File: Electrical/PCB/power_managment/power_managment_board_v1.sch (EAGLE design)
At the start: 0 parts

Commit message: Started schematic for boost converter
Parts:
- added U$1: LMR64010SOT, RobotRacing2019_Master:LMR64010SOT

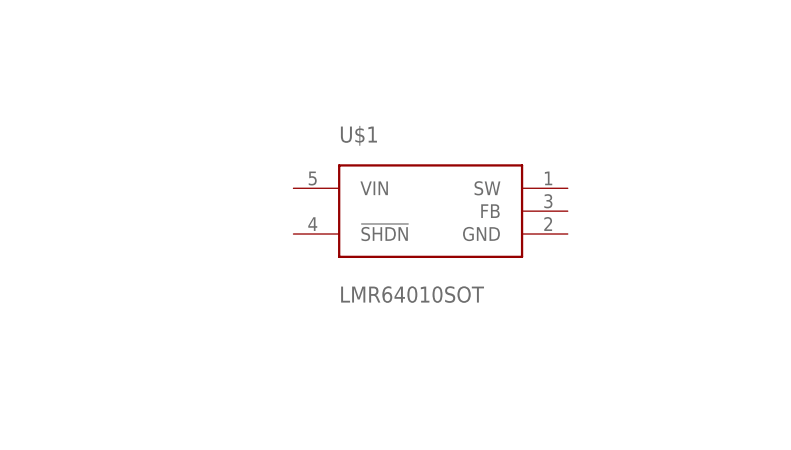
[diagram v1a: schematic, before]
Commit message: Imported a diode library
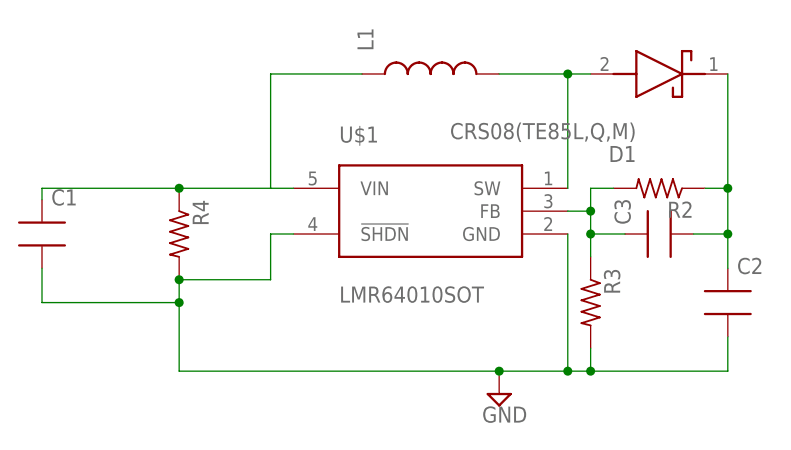
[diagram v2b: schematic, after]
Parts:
- added C1, C2, C3: (no value), RobotRacing2019_Master:CAP0603
- added D1: CRS08(TE85L,Q,M), SamacSys_Parts:CRS08(TE85L,Q,M)
- added L1: (no value), RobotRacing2019_Master:IND0603
- added R2, R3, R4: (no value), RobotRacing2019_Master:RES0603
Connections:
- new net GND: C1.2, C2.2, R3.2, R4.2, U$1.!SHDN, U$1.GND
- new net N$1: C1.1, L1.1, R4.1, U$1.VIN
- new net N$2: C2.1, C3.2, D1.K, R2.1
- new net N$3: C3.1, R2.2, R3.1, U$1.FB
- new net N$4: D1.A, L1.2, U$1.SW
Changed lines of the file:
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@@
 <parts>
 <part name="U$1" library="RobotRacing2019_Master" deviceset="LMR64010" device="SOT"/>
+<part name="C1" library="RobotRacing2019_Master" deviceset="CAP0603" device=""/>
+<part name="C2" library="RobotRacing2019_Master" deviceset="CAP0603" device=""/>
+<part name="C3" library="RobotRacing2019_Master" deviceset="CAP0603" device=""/>
+<part name="R2" library="RobotRacing2019_Master" deviceset="RES0603" device=""/>
+<part name="R3" library="RobotRacing2019_Master" deviceset="RES0603" device=""/>
+<part name="R4" library="RobotRacing2019_Master" deviceset="RES0603" device=""/>
+<part name="SUPPLY1" library="RobotRacing2019_Master" deviceset="GND" device=""/>
+<part name="L1" library="RobotRacing2019_Master" deviceset="IND0603" device=""/>
+<part name="D1" library="SamacSys_Parts" deviceset="CRS08(TE85L,Q,M)" device=""/>
 </parts>
 <sheets>
@@
 <attribute name="VALUE" x="-10.16" y="-10.16" size="1.778" layer="96"/>
 </instance>
+<instance part="C1" gate="G$1" x="-43.18" y="-2.54" smashed="yes">
+<attribute name="NAME" x="-42.164" y="0.635" size="1.778" layer="95"/>
+<attribute name="VALUE" x="-42.164" y="-6.731" size="1.778" layer="96"/>
+</instance>
+<instance part="C2" gate="G$1" x="33.02" y="-10.16" smashed="yes">
+<attribute name="NAME" x="34.036" y="-6.985" size="1.778" layer="95"/>
+<attribute name="VALUE" x="34.036" y="-14.351" size="1.778" layer="96"/>
+</instance>
+<instance part="C3" gate="G$1" x="25.4" y="-2.54" smashed="yes" rot="R90">
+<attribute name="NAME" x="22.225" y="-1.524" size="1.778" layer="95" rot="R90"/>
+<attribute name="VALUE" x="29.591" y="-1.524" size="1.778" layer="96" rot="R90"/>
+</instance>
+<instance part="R2" gate="G$1" x="25.4" y="2.54" smashed="yes" rot="R180">
+<attribute name="NAME" x="29.21" y="1.0414" size="1.778" layer="95" rot="R180"/>
+<attribute name="VALUE" x="29.21" y="5.842" size="1.778" layer="96" rot="R180"/>
+</instance>
+<instance part="R3" gate="G$1" x="17.78" y="-10.16" smashed="yes" rot="R270">
+<attribute name="NAME" x="19.2786" y="-6.35" size="1.778" layer="95" rot="R270"/>
+<attribute name="VALUE" x="14.478" y="-6.35" size="1.778" layer="96" rot="R270"/>
+</instance>
+<instance part="R4" gate="G$1" x="-27.94" y="-2.54" smashed="yes" rot="R270">
+<attribute name="NAME" x="-26.4414" y="1.27" size="1.778" layer="95" rot="R270"/>
+<attribute name="VALUE" x="-31.242" y="1.27" size="1.778" layer="96" rot="R270"/>
+</instance>
+<instance part="SUPPLY1" gate="GND" x="7.62" y="-20.32" smashed="yes">
+<attribute name="VALUE" x="5.715" y="-23.495" size="1.778" layer="96"/>
+</instance>
+<instance part="L1" gate="G$1" x="0" y="15.24" smashed="yes" rot="R90">
+<attribute name="NAME" x="-6.35" y="17.78" size="1.778" layer="95" rot="R90"/>
+<attribute name="VALUE" x="6.35" y="17.78" size="1.778" layer="96" rot="R90"/>
+</instance>
+<instance part="D1" gate="G$1" x="35.56" y="15.24" smashed="yes" rot="R180">
+<attribute name="NAME" x="22.86" y="6.35" size="1.778" layer="95" rot="R180" align="center-left"/>
+<attribute name="VALUE" x="22.86" y="8.89" size="1.778" layer="96" rot="R180" align="center-left"/>
+</instance>
 </instances>
 <busses>
 </busses>
 <nets>
+<net name="N$1" class="0">
+<segment>
+<pinref part="U$1" gate="G$1" pin="VIN"/>
+<pinref part="R4" gate="G$1" pin="1"/>
+<wire x1="-15.24" y1="2.54" x2="-17.78" y2="2.54" width="0.1524" layer="91"/>
+<pinref part="C1" gate="G$1" pin="1"/>
+<wire x1="-43.18" y1="1.27" x2="-43.18" y2="2.54" width="0.1524" layer="91"/>
+<wire x1="-43.18" y1="2.54" x2="-27.94" y2="2.54" width="0.1524" layer="91"/>
+<junction x="-27.94" y="2.54"/>
+<wire x1="-27.94" y1="2.54" x2="-17.78" y2="2.54" width="0.1524" layer="91"/>
+<wire x1="-17.78" y1="2.54" x2="-17.78" y2="15.24" width="0.1524" layer="91"/>
+<pinref part="L1" gate="G$1" pin="1"/>
+<wire x1="-17.78" y1="15.24" x2="-7.62" y2="15.24" width="0.1524" layer="91"/>
+</segment>
+</net>
+<net name="GND" class="0">
+<segment>
+<pinref part="U$1" gate="G$1" pin="GND"/>
+<pinref part="SUPPLY1" gate="GND" pin="GND"/>
+<wire x1="15.24" y1="-2.54" x2="15.24" y2="-17.78" width="0.1524" layer="91"/>
+<wire x1="15.24" y1="-17.78" x2="7.62" y2="-17.78" width="0.1524" layer="91"/>
+<wire x1="15.24" y1="-17.78" x2="17.78" y2="-17.78" width="0.1524" layer="91"/>
+<junction x="15.24" y="-17.78"/>
+<pinref part="R3" gate="G$1" pin="2"/>
+<wire x1="17.78" y1="-17.78" x2="17.78" y2="-15.24" width="0.1524" layer="91"/>
+<pinref part="R4" gate="G$1" pin="2"/>
+<wire x1="-27.94" y1="-7.62" x2="-17.78" y2="-7.62" width="0.1524" layer="91"/>
+<wire x1="-17.78" y1="-7.62" x2="-17.78" y2="-2.54" width="0.1524" layer="91"/>
+<pinref part="U$1" gate="G$1" pin="!SHDN"/>
+<wire x1="-17.78" y1="-2.54" x2="-15.24" y2="-2.54" width="0.1524" layer="91"/>
+<pinref part="C1" gate="G$1" pin="2"/>
+<wire x1="-43.18" y1="-6.35" x2="-43.18" y2="-10.16" width="0.1524" layer="91"/>
+<wire x1="-43.18" y1="-10.16" x2="-27.94" y2="-10.16" width="0.1524" layer="91"/>
+<wire x1="-27.94" y1="-10.16" x2="-27.94" y2="-7.62" width="0.1524" layer="91"/>
+<junction x="-27.94" y="-7.62"/>
+<wire x1="-27.94" y1="-10.16" x2="-27.94" y2="-17.78" width="0.1524" layer="91"/>
+<junction x="-27.94" y="-10.16"/>
+<wire x1="-27.94" y1="-17.78" x2="7.62" y2="-17.78" width="0.1524" layer="91"/>
+<junction x="7.62" y="-17.78"/>
+<pinref part="C2" gate="G$1" pin="2"/>
+<wire x1="17.78" y1="-17.78" x2="33.02" y2="-17.78" width="0.1524" layer="91"/>
+<wire x1="33.02" y1="-17.78" x2="33.02" y2="-13.97" width="0.1524" layer="91"/>
+<junction x="17.78" y="-17.78"/>
+</segment>
+</net>
+<net name="N$2" class="0">
+<segment>
+<pinref part="C3" gate="G$1" pin="2"/>
+<pinref part="C2" gate="G$1" pin="1"/>
+<wire x1="29.21" y1="-2.54" x2="33.02" y2="-2.54" width="0.1524" layer="91"/>
+<wire x1="33.02" y1="-2.54" x2="33.02" y2="-6.35" width="0.1524" layer="91"/>
+<pinref part="R2" gate="G$1" pin="1"/>
+<wire x1="30.48" y1="2.54" x2="33.02" y2="2.54" width="0.1524" layer="91"/>
+<wire x1="33.02" y1="2.54" x2="33.02" y2="-2.54" width="0.1524" layer="91"/>
+<junction x="33.02" y="-2.54"/>
+<pinref part="D1" gate="G$1" pin="K"/>
+<wire x1="33.02" y1="15.24" x2="33.02" y2="2.54" width="0.1524" layer="91"/>
+<junction x="33.02" y="2.54"/>
+</segment>
+</net>
+<net name="N$3" class="0">
+<segment>
+<pinref part="R3" gate="G$1" pin="1"/>
+<wire x1="17.78" y1="-5.08" x2="17.78" y2="-2.54" width="0.1524" layer="91"/>
+<pinref part="U$1" gate="G$1" pin="FB"/>
+<wire x1="17.78" y1="-2.54" x2="17.78" y2="0" width="0.1524" layer="91"/>
+<wire x1="17.78" y1="0" x2="15.24" y2="0" width="0.1524" layer="91"/>
+<pinref part="C3" gate="G$1" pin="1"/>
+<wire x1="21.59" y1="-2.54" x2="17.78" y2="-2.54" width="0.1524" layer="91"/>
+<junction x="17.78" y="-2.54"/>
+<pinref part="R2" gate="G$1" pin="2"/>
+<wire x1="20.32" y1="2.54" x2="17.78" y2="2.54" width="0.1524" layer="91"/>
+<wire x1="17.78" y1="2.54" x2="17.78" y2="0" width="0.1524" layer="91"/>
+<junction x="17.78" y="0"/>
+</segment>
+</net>
+<net name="N$4" class="0">
+<segment>
+<pinref part="L1" gate="G$1" pin="2"/>
+<pinref part="U$1" gate="G$1" pin="SW"/>
+<wire x1="7.62" y1="15.24" x2="15.24" y2="15.24" width="0.1524" layer="91"/>
+<wire x1="15.24" y1="15.24" x2="15.24" y2="2.54" width="0.1524" layer="91"/>
+<pinref part="D1" gate="G$1" pin="A"/>
+<wire x1="15.24" y1="15.24" x2="17.78" y2="15.24" width="0.1524" layer="91"/>
+<junction x="15.24" y="15.24"/>
+</segment>
+</net>
 </nets>
 </sheet>

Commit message: Updated the SVS for 11.1V
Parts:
- added C4: 2.2uF, RobotRacing2019_Master:CAP0603
- added C5: 4.7uF, RobotRacing2019_Master:CAP0603
- added C6: 160pF, RobotRacing2019_Master:CAP0603
- added C7: TBA (Probably OPEN), RobotRacing2019_Master:CAP0603
- added C8: TBA, RobotRacing2019_Master:CAP0603
- added D2: CRS08(TE85L,Q,M), SamacSys_Parts:CRS08(TE85L,Q,M)
- added L2: 10uH, RobotRacing2019_Master:IND0603
- added R1: 124k, RobotRacing2019_Master:RES0603
- added R5: 13.3k, RobotRacing2019_Master:RES0603
- added R6: 51k, RobotRacing2019_Master:RES0603
- added R7: 100k, RobotRacing2019_Master:RES0603
- added U$2: LMR64010SOT, RobotRacing2019_Master:LMR64010SOT
- added U$3: S-1011AA0SOT, RobotRacing2019_Master:S-1011AA0SOT
- C1: value (none) -> 2.2uF
- C2: value (none) -> 4.7uF
- C3: value (none) -> 160pF
- L1: value (none) -> 10uH
- R2: value (none) -> 124k
- R3: value (none) -> 13.3k
- R4: value (none) -> 51k
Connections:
- removed net N$1: C1.1, L1.1, R4.1, U$1.VIN
- new net N$10: R7.1, U$3.OUT
- new net N$12: C8.1, U$3.CN
- new net N$13: C7.1, U$3.CP
- new net N$6: C5.1, C6.2, D2.K, R1.1
- new net N$7: C6.1, R1.2, R5.1, U$2.FB
- new net N$8: D2.A, L2.2, U$2.SW
- new net VDD: C1.1, C4.1, L1.1, L2.1, R4.1, R6.1, R7.2, U$1.VIN, U$2.VIN, U$3.VDD
- net GND: now also C4.2, C5.2, C7.2, C8.2, R5.2, R6.2, U$2.!SHDN, U$2.GND, U$3.VSS
